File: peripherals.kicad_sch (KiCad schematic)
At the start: 16 parts, among them J10 Cam 3, J11 Servo, J12 Cam 2, J2 Encoder, J9 Cam 1, Q1 BSS816NWH6327XTSA1, Q2 NPN, Q3 BSS816NWH6327XTSA1, Q5 BSS816NWH6327XTSA1

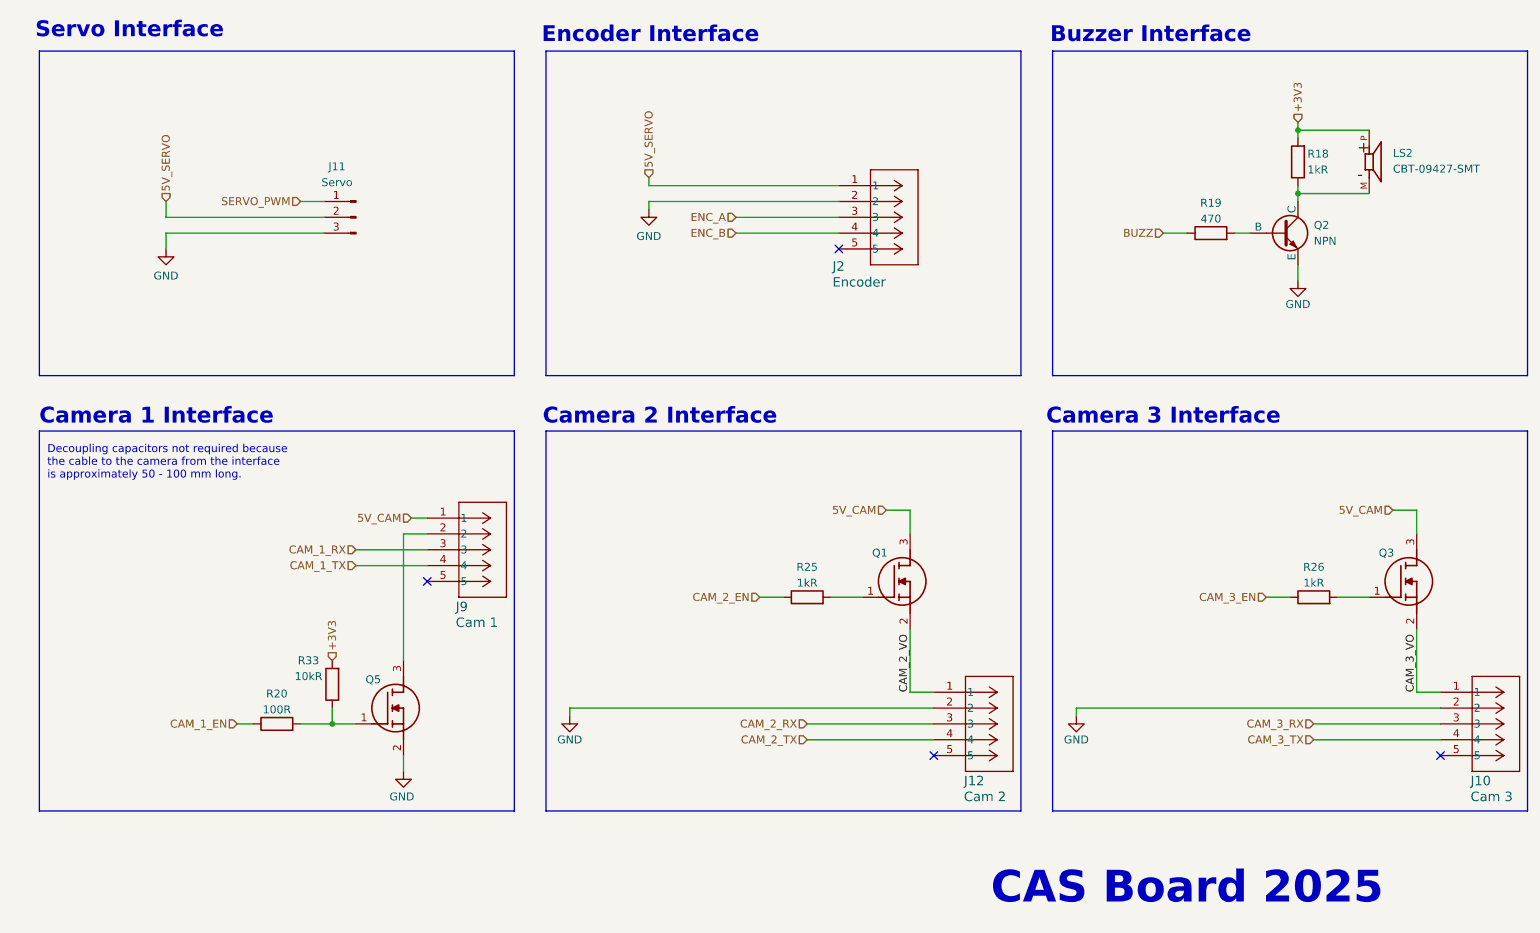
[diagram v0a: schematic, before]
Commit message: Update cam 2 and cam 3 schematic
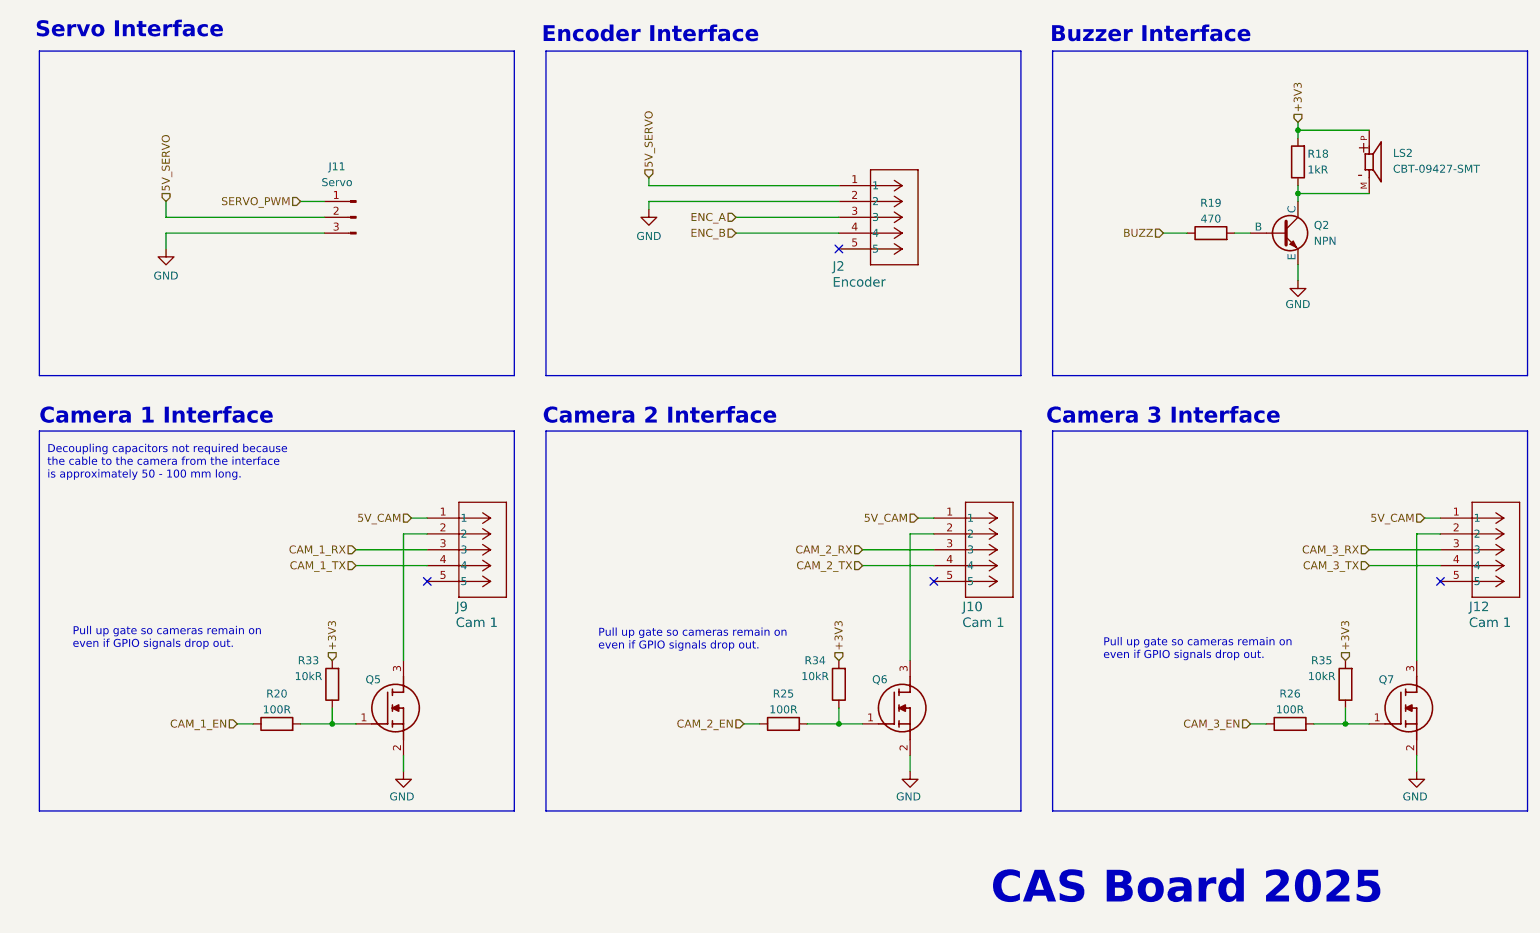
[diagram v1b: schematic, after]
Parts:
- removed Q1, Q3: BSS816NWH6327XTSA1, SOT65P210X100-3N, symbol BSS816NWH6327XTSA1:BSS816NWH6327XTSA1
- added Q6, Q7: BSS816NWH6327XTSA1, SOT65P210X100-3N, symbol BSS816NWH6327XTSA1:BSS816NWH6327XTSA1
- added R34, R35: 10kR, Resistor_SMD:R_0805_2012Metric_Pad1.20x1.40mm_HandSolder, symbol Device:R
- J10: value Cam 3 -> Cam 1
- J12: value Cam 2 -> Cam 1
- R25, R26: value 1kR -> 100R
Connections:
- net CAM_2_VO is gone; now on net 5V_CAM: J12.1
- net CAM_3_VO is gone; now on net 5V_CAM: J10.1
- net +3V3: now also R34.2, R35.2
- net CAM_2_RX: now also J10.3; no longer J12.3
- net CAM_2_TX: now also J10.4; no longer J12.4
- net CAM_3_RX: now also J12.3; no longer J10.3
- net CAM_3_TX: now also J12.4; no longer J10.4
- net GND: now also Q6.2 (S), Q7.2 (S); no longer J10.2, J12.2
- net at R25.2: now also Q6.1 (G), R34.1
- net at R26.2: now also Q7.1 (G), R35.1
- new net: J10.2, Q6.3 (D)
- new net: J12.2, Q7.3 (D)
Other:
- note added: "Pull up gate so cameras remain on even if GPIO signals drop out."

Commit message: sync
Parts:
- LS2: footprint CBT-09427-SMT:CUI_CBT-09427-SMT -> CBT_09427_SMT_TR:CUI_CBT-09427-SMT
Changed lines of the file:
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@@
 			)
 		)
-		(property "Footprint" "CBT-09427-SMT:CUI_CBT-09427-SMT"
+		(property "Footprint" "CBT_09427_SMT_TR:CUI_CBT-09427-SMT"
 			(at 238.76 57.15 0)
 			(effects

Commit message: Sync
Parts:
- J11: footprint Connector_PinHeader_2.54mm:PinHeader_1x03_P2.54mm_Vertical -> B3B_XH_A:JST_B3B-XH-A
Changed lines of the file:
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@@
 			)
 		)
-		(property "Footprint" "Connector_PinHeader_2.54mm:PinHeader_1x03_P2.54mm_Vertical"
+		(property "Footprint" "B3B_XH_A:JST_B3B-XH-A"
 			(at 76.2 66.04 0)
 			(effects

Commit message: Sync layout
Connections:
- net 5V_CAM: now also J2.1
- net 5V_SERVO: no longer J2.1
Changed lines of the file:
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@@
 		)
 	)
-	(hierarchical_label "5V_SERVO"
+	(hierarchical_label "5V_CAM"
 		(shape input)
 		(at 123.19 59.69 90)

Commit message: Sync more routing
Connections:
- net GND: now also J11.1 (Pin_1); no longer J11.3 (Pin_3)
- net SERVO_PWM: now also J11.3 (Pin_3); no longer J11.1 (Pin_1)
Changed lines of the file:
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@@
 	(wire
 		(pts
+			(xy 57.15 58.42) (xy 50.8 58.42)
+		)
+		(stroke
+			(width 0)
+			(type default)
+		)
+	)
+	(wire
+		(pts
+			(xy 45.72 68.58) (xy 71.12 68.58)
+		)
+		(stroke
+			(width 0)
+			(type default)
+		)
+	)
+	(wire
+		(pts
 			(xy 250.19 114.3) (xy 247.65 114.3)
 		)
@@
 		)
 	)
+	(wire
+		(pts
+			(xy 50.8 58.42) (xy 50.8 59.69)
+		)
+		(stroke
+			(width 0)
+			(type default)
+		)
+	)
 	(polyline
 		(pts
@@
 		)
 	)
-	(wire
-		(pts
-			(xy 45.72 63.5) (xy 45.72 66.04)
-		)
-		(stroke
-			(width 0)
-			(type default)
-		)
-	)
 	(polyline
 		(pts
@@
 	(wire
 		(pts
-			(xy 71.12 68.58) (xy 45.72 68.58)
+			(xy 71.12 63.5) (xy 57.15 63.5)
 		)
 		(stroke
@@
 	(wire
 		(pts
-			(xy 67.31 63.5) (xy 71.12 63.5)
-		)
-		(stroke
-			(width 0)
-			(type default)
-		)
-	)
-	(wire
-		(pts
-			(xy 45.72 68.58) (xy 45.72 71.12)
+			(xy 57.15 63.5) (xy 57.15 58.42)
 		)
 		(stroke
@@
 	(hierarchical_label "5V_SERVO"
 		(shape input)
-		(at 45.72 63.5 90)
+		(at 45.72 66.04 180)
 		(effects
 			(font
 				(size 1.27 1.27)
 			)
-			(justify left)
+			(justify right)
 		)
 	)
@@
 	(hierarchical_label "SERVO_PWM"
 		(shape input)
-		(at 67.31 63.5 180)
+		(at 45.72 68.58 180)
 		(effects
 			(font
@@
 	(symbol
 		(lib_id "power:GND")
-		(at 45.72 71.12 0)
+		(at 50.8 59.69 0)
 		(unit 1)
 		(exclude_from_sim no)
@@
 		(dnp no)
 		(property "Reference" "#PWR051"
-			(at 45.72 77.47 0)
+			(at 50.8 66.04 0)
 			(effects
 				(font
@@
 		)
 		(property "Value" "GND"
-			(at 45.72 75.438 0)
+			(at 50.8 64.008 0)
 			(effects
 				(font
@@
 		)
 		(property "Footprint" ""
-			(at 45.72 71.12 0)
+			(at 50.8 59.69 0)
 			(effects
 				(font
@@
 		)
 		(property "Datasheet" ""
-			(at 45.72 71.12 0)
+			(at 50.8 59.69 0)
 			(effects
 				(font
@@
 		)
 		(property "Description" "Power symbol creates a global label with name \"GND\" , ground"
-			(at 45.72 71.12 0)
+			(at 50.8 59.69 0)
 			(effects
 				(font
